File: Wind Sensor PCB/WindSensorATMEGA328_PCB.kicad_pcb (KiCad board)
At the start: 2 copper layers, 44.9 x 44.9 mm, 38 parts, among them P10 I2C, P11 WIND_A, P2 SERIAL, P3 ID, P4 ISP, P5 LOGO2, P6 PCB, P8 VANE, P9 PROG, SW1 SWA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

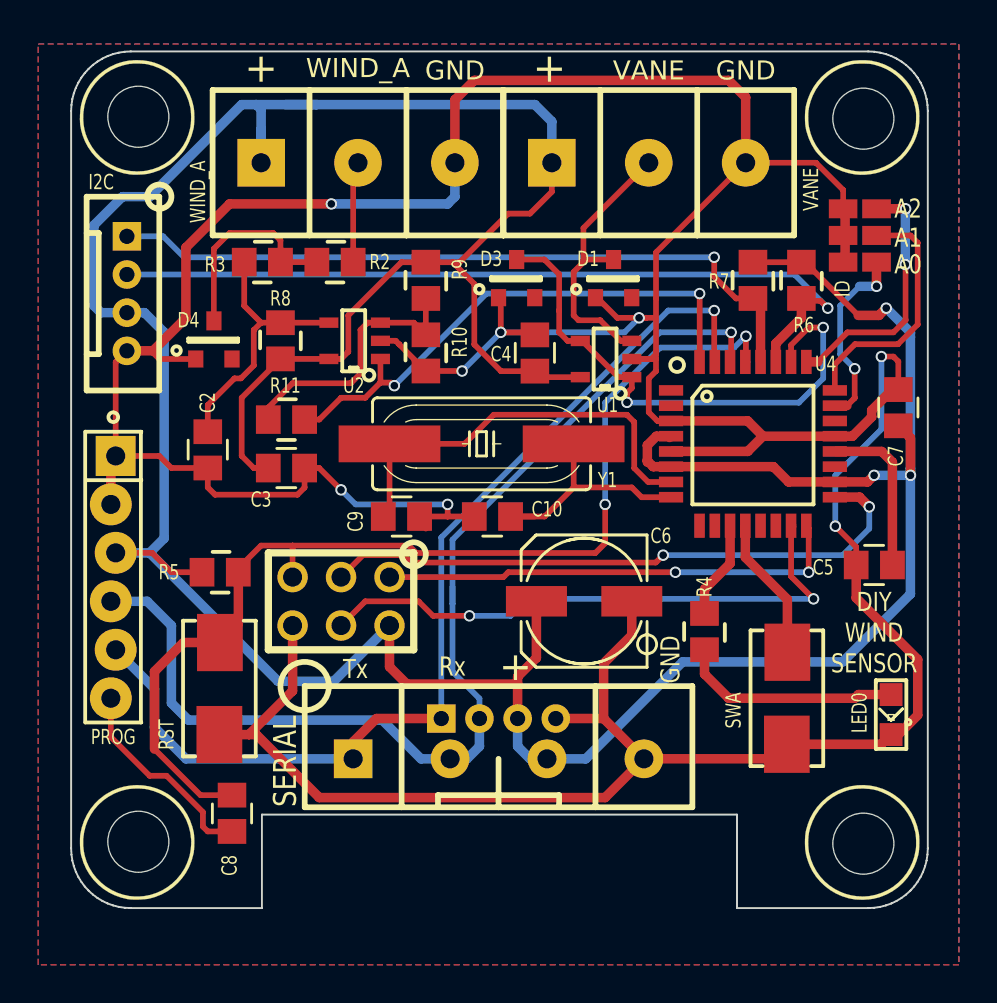
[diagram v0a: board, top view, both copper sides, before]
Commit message: Update of PCB to add LPF on inputs
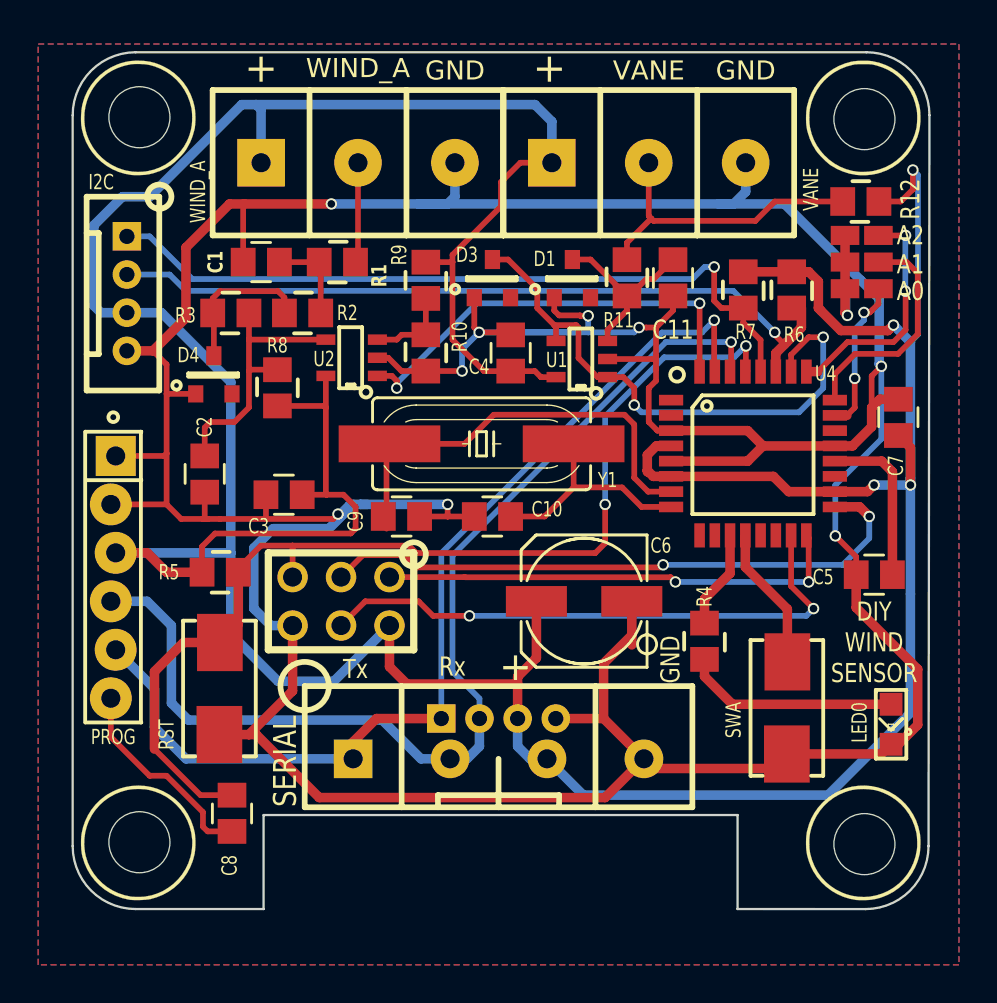
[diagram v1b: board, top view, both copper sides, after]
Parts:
- added C1: 100n, REInnovationFootprint:SM_C_0805, F.Cu at (136.1, 100.3)
- added C11: 100n, REInnovationFootprint:SM_C_0805, F.Cu at (157.7, 101.2)
- added R1: 10k, REInnovationFootprint:SM0805, F.Cu at (140.1, 100.3)
- added R12: 10k, REInnovationFootprint:SM0805, F.Cu at (167.6, 97.2)
- P6: footprint REInnovationFootprint:PCB_45_45_Cut_Out_Solar_Sensor -> REInnovationFootprint:PCB_45_45_Cut_Out_Solar_Sensor_2
- R11: value 4M7 -> 10k
- R8: value 100k -> 470k
- moved R11 19.3 mm to (155.3, 101.2), turned to 180 degrees
- moved R2 3.16 mm to (138.3, 103.0)
- moved R3 3.12 mm to (134.6, 103.0), turned to -90 degrees
- moved R8 2.47 mm to (137.0, 106.9)
- moved D1 2.16 mm to (152.5, 101.2)
- moved D4 1.83 mm to (133.7, 106.2)
- moved C3 1.40 mm to (137.3, 112.5)
- moved P3 1.40 mm to (168.5, 99.2)
- moved C2 1.28 mm to (133.2, 111.4)
- moved C4 1.27 mm to (149.2, 105.1)
- moved D3 1.27 mm to (148.3, 101.2)
- moved U1 1.27 mm to (154.3, 105.4)
- moved U2 0.90 mm to (142.2, 105.3)
- moved R6 0.71 mm to (164.0, 101.8)
- moved R7 0.71 mm to (161.4, 101.8)
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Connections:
- net /ATMega328/D7_LED0 renamed /ATMega328/D7
- net /ATMega328/D8_SWA renamed /ATMega328/D8
- C3 pad 1: VCC -> GND
- C3 pad 2: GND -> VCC
- D1 pad 2: /Wind_Vane/WIND_V_SIG -> Net-(D1-K)
- R10 pad 2: Net-(R10-Pad2) -> Net-(U2-+)
- R11 pad 1: Net-(R10-Pad2) -> Net-(D1-K)
- R11 pad 2: /WIND_FREQ -> /Wind_Vane/WIND_V_SIG
- R2 pad 2: /Hall_to_Freq/WIND_A_SIG -> Net-(C1-Pad2)
- R9 pad 2: Net-(R10-Pad2) -> Net-(U2-+)
- U1 pad 3: /Wind_Vane/WIND_V_SIG -> Net-(D1-K)
- U2 pad 3: Net-(R10-Pad2) -> Net-(U2-+)
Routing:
- net VCC: track 204.6 -> 233.2 mm, vias 3 -> 4
- net GND: track 236.8 -> 262.3 mm, vias 8 -> 10
- net Net-(R10-Pad2): track 14.2 -> 0.00 mm
- net Net-(D1-K): track 0.00 -> 9.63 mm
- net /WIND_FREQ: track 28.4 -> 23.0 mm
- net Net-(C1-Pad2): track 0.00 -> 4.79 mm
- net Net-(U2-+): track 0.00 -> 4.55 mm
- net /I2C_SDA: track 43.1 -> 39.9 mm
- net Net-(D4-K): track 10.8 -> 7.90 mm
- net /ATMega328/A0: track 10.0 -> 8.13 mm
- net /Rx: track 58.4 -> 56.8 mm
- net /WIND_VANE: track 28.2 -> 29.7 mm
- net /Wind_Vane/WIND_V_SIG: track 14.9 -> 16.2 mm
- net /ATMega328/A1: track 13.2 -> 12.1 mm
- net Net-(U4-XTAL2/PB7): track 12.8 -> 11.8 mm
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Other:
- outline, holes or cut-outs redrawn
- net class Default removed

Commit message: Large update - firmware and PCB design. V2
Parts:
- D1: value 5V1_Zener -> 3V3_Zener
- R6, R7: value 10k -> 4k7
